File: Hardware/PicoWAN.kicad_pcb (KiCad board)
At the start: 2 copper layers, 50.8 x 22.9 mm, 9 parts, among them J1 Conn_Battery, J3 Conn_left, J4 Conn_right, P1 USB_C_Plug_USB2.0

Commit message: init select footprints
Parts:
- added AE1: Antenna_Shield, Jumper:SolderJumper-2_P1.3mm_Bridged2Bar_Pad1.0x1.5mm, F.Cu at (175.8, 98.0)
- added C1: 22pF, Capacitor_SMD:C_0805_2012Metric, F.Cu at (174.2, 62.7)
- added C10: 0.1uF, Capacitor_SMD:C_0805_2012Metric, F.Cu at (169.7, 61.6)
- added C11: 0.1uF, Capacitor_SMD:C_0805_2012Metric, F.Cu at (172.2, 50.6)
- added C12: 0.1uF, Capacitor_SMD:C_0805_2012Metric, F.Cu at (172.2, 53.6)
- added C13: 0.1uF, Capacitor_SMD:C_0805_2012Metric, F.Cu at (164.9, 58.6)
- added C14: 0.1uF, Capacitor_SMD:C_0805_2012Metric, F.Cu at (159.7, 66.5)
- added C15: 0.1uF, Capacitor_SMD:C_0805_2012Metric, F.Cu at (165.3, 61.6)
- added C16: 10uF, Capacitor_SMD:C_0805_2012Metric, F.Cu at (169.4, 58.6)
- added C17: 10uF, Capacitor_SMD:C_0805_2012Metric, F.Cu at (176.7, 50.6)
- added C18: 0.1uF, Capacitor_SMD:C_0805_2012Metric, F.Cu at (176.7, 53.6)
- added C19: 0.1uF, Capacitor_SMD:C_0805_2012Metric, F.Cu at (165.3, 64.6)
- added C2: 22pF, Capacitor_SMD:C_0805_2012Metric, F.Cu at (178.3, 56.6)
- added C3: 1uF, Capacitor_SMD:C_0805_2012Metric, F.Cu at (174.2, 59.7)
- added C4: 0.1uF, Capacitor_SMD:C_0805_2012Metric, F.Cu at (169.7, 64.6)
- added C5: 4.7uF, Capacitor_SMD:C_0805_2012Metric, F.Cu at (164.2, 67.7)
- added C6: 0.1uF, Capacitor_SMD:C_0805_2012Metric, F.Cu at (173.8, 56.6)
- added C7: 1uF, Capacitor_SMD:C_0805_2012Metric, F.Cu at (159.7, 69.5)
- added C8: 1uF, Capacitor_SMD:C_0805_2012Metric, F.Cu at (178.6, 59.7)
- added C9: 0.1uF, Capacitor_SMD:C_0805_2012Metric, F.Cu at (168.6, 67.7)
- added D1: MBR120, Diode_SMD:D_SOD-123F, F.Cu at (167.3, 50.8)
- added D2: LED, LED_SMD:LED_0805_2012Metric_Pad1.15x1.40mm_HandSolder, F.Cu at (160.7, 63.4)
- added D3: LED, LED_SMD:LED_0805_2012Metric, F.Cu at (181.1, 50.6)
- added R1: 100K, Resistor_SMD:R_0805_2012Metric, F.Cu at (181.1, 53.6)
- added R10: 10K, Resistor_SMD:R_0805_2012Metric, F.Cu at (150.1, 58.4)
- added R11: 5K1, Resistor_SMD:R_0805_2012Metric, F.Cu at (156.6, 52.7)
- added R12: 5K1, Resistor_SMD:R_0805_2012Metric, F.Cu at (154.5, 58.4)
- added R2: 1K, Resistor_SMD:R_0805_2012Metric, F.Cu at (182.7, 56.6)
- added R3: 10K, Resistor_SMD:R_0805_2012Metric, F.Cu at (173.1, 67.6)
- added R4: 27, Resistor_SMD:R_0805_2012Metric, F.Cu at (178.6, 62.6)
- added R5: 27, Resistor_SMD:R_0805_2012Metric, F.Cu at (183.1, 59.5)
- added R6: 2K, Resistor_SMD:R_0805_2012Metric, F.Cu at (177.5, 65.6)
- added R7: 1K, Resistor_SMD:R_0805_2012Metric, F.Cu at (183.0, 62.6)
- added R8: 10K, Resistor_SMD:R_0805_2012Metric, F.Cu at (177.5, 68.6)
- added R9: 1K, Resistor_SMD:R_0805_2012Metric, F.Cu at (181.9, 65.6)
- added U1: AP2112K-3.3, Package_TO_SOT_SMD:SOT-23-5, F.Cu at (138.4, 92.5)
- added U2: RP2040, Package_DFN_QFN:QFN-56-1EP_7x7mm_P0.4mm_EP5.6x5.6mm_ThermalVias, F.Cu at (148.1, 92.7)
- added U3: MCP73831-2-OT, Package_TO_SOT_SMD:SOT-23-5, F.Cu at (138.4, 98.3)
- added U4: W25Q32JVZP, Package_SON:WSON-8-1EP_6x5mm_P1.27mm_EP3.4x4.3mm, F.Cu at (134.9, 71.4)
- added U5: RFM95W-868S2, RF_Module:HOPERF_RFM9XW_SMD, F.Cu at (163.8, 92.7)
- G***: moved to B.Cu
- moved P1 8.14 mm to (131.8, 93.2)
- moved J1 7.88 mm to (137.4, 84.1)
- turned G*** to 180 degrees
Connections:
- J3 pad 10: /A5 -> /D25
- J3 pad 11: /SCK -> /SCK_0
- J3 pad 12: /MOSI -> /COPI_0
- J3 pad 13: /MISO -> /CIPO_0
- J3 pad 16: GND -> /D4
- J3 pad 3: /AREF -> +3V3
- J3 pad 9: /A4 -> /D24

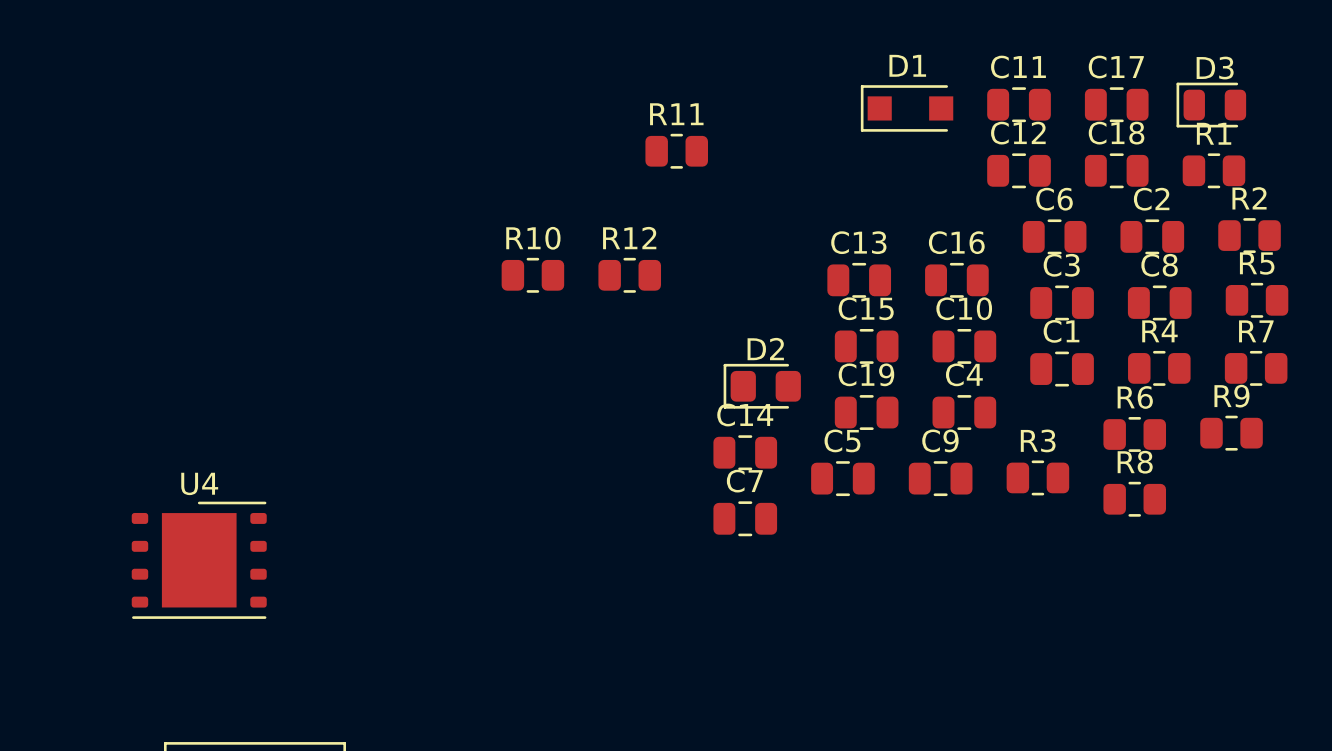
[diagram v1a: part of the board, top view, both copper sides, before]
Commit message: update to 0603
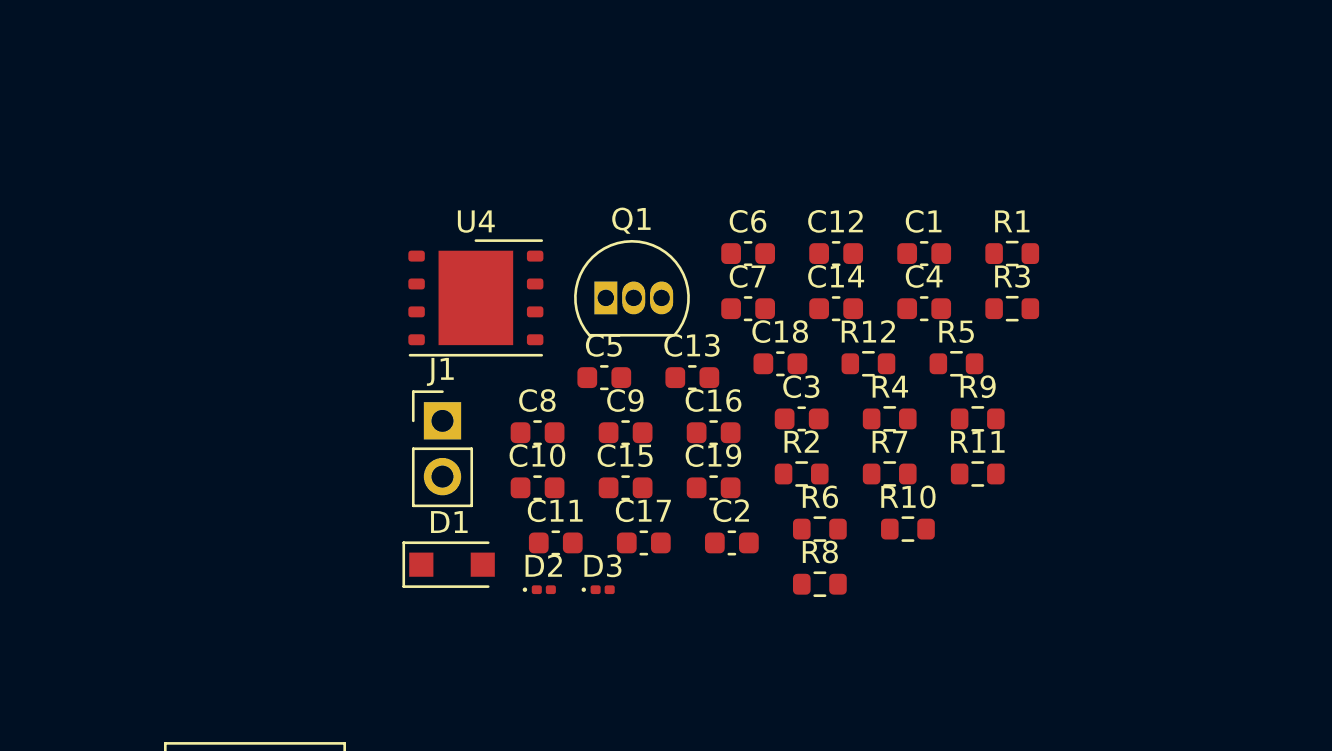
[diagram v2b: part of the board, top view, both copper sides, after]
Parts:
- added J1: Battery, Connector_PinHeader_2.54mm:PinHeader_1x02_P2.54mm_Vertical, F.Cu at (146.0, 65.0)
- added Q1: DMG3415U-7, Package_TO_SOT_THT:TO-92L_Inline, F.Cu at (153.4, 59.4)
- C1, C10, C11, C12, C13, C14, C15, C16, C17, C18, C19, C2, C3, C4, C5, C6, C7, C8, C9: footprint Capacitor_SMD:C_0805_2012Metric -> Capacitor_SMD:C_0603_1608Metric
- D2: footprint LED_SMD:LED_0805_2012Metric_Pad1.15x1.40mm_HandSolder -> LED_SMD:LED_0201_0603Metric
- D3: footprint LED_SMD:LED_0805_2012Metric -> LED_SMD:LED_0201_0603Metric
- R1, R10, R11, R12, R2, R3, R4, R5, R6, R7, R8, R9: footprint Resistor_SMD:R_0805_2012Metric -> Resistor_SMD:R_0603_1608Metric
- moved D3 35.6 mm to (153.2, 72.7)
- moved D1 29.5 mm to (146.4, 71.6)
- moved C17 29.4 mm to (155.1, 70.6)
- moved C11 29.0 mm to (151.1, 70.6)
- moved C8 28.9 mm to (150.3, 65.6)
- moved C2 23.7 mm to (159.1, 70.6)
- moved R2 23.1 mm to (162.3, 67.4)
- moved R10 20.6 mm to (167.2, 70.0)
- moved C10 20.5 mm to (150.3, 68.1)
- moved R11 20.1 mm to (170.3, 67.4)
- moved C18 17.7 mm to (161.3, 62.4)
- moved R7 17.4 mm to (166.3, 67.4)
- moved U4 17.4 mm to (147.5, 59.4)
- moved R6 15.0 mm to (163.1, 70.0)
- moved R8 14.9 mm to (163.1, 72.5)
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
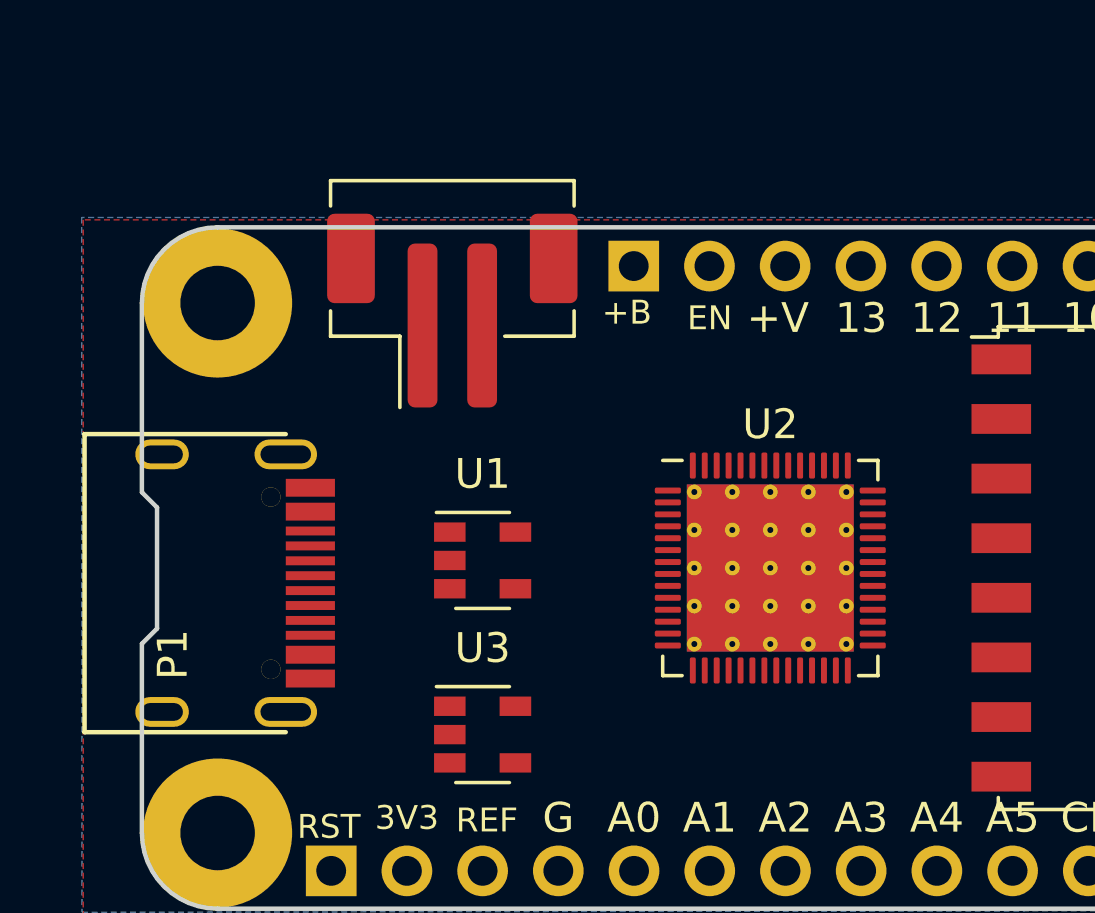
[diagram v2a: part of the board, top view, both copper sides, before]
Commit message: update footprint RP2040
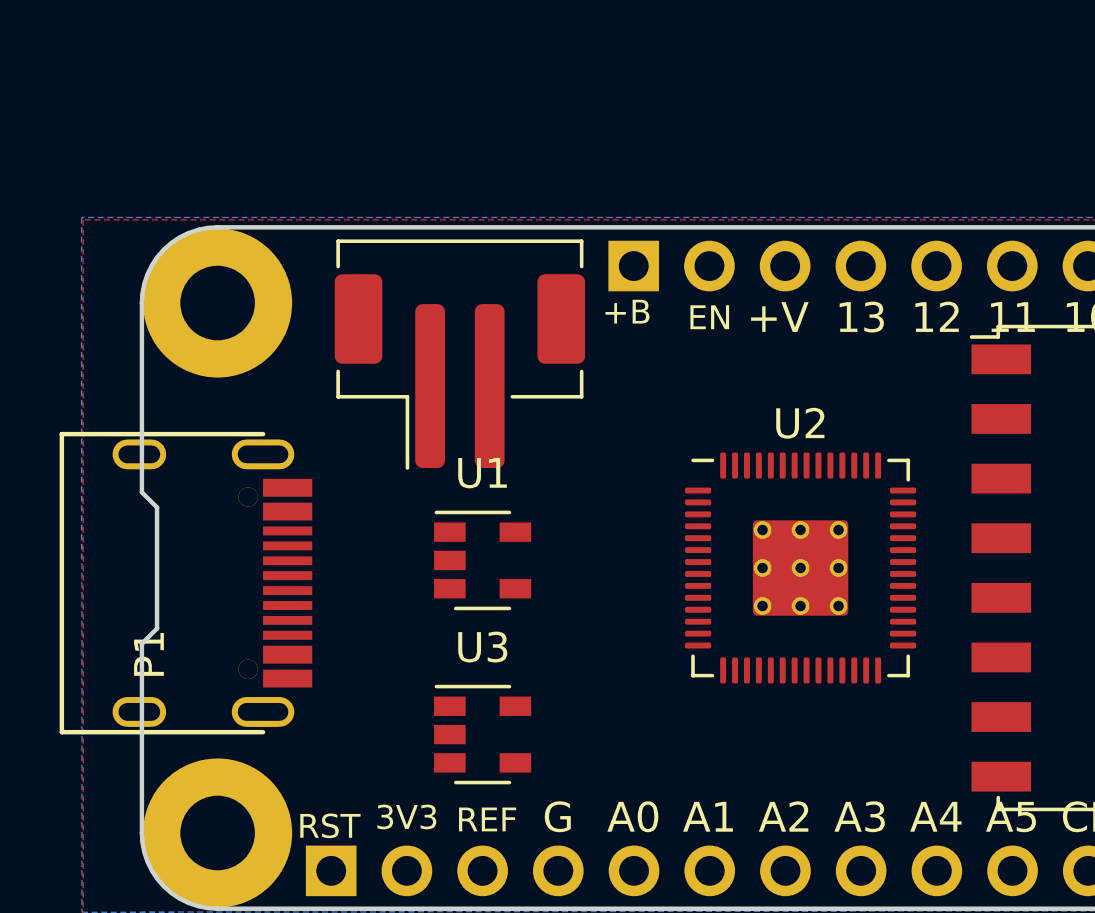
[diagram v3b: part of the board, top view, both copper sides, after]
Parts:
- U2: footprint Package_DFN_QFN:QFN-56-1EP_7x7mm_P0.4mm_EP5.6x5.6mm_ThermalVias -> MCU_RaspberryPi_and_Boards:RP2040-QFN-56
- moved J1 2.05 mm to (137.7, 86.1)
- moved U2 1.02 mm to (149.1, 92.7)
- moved P1 0.76 mm to (131.1, 93.2)

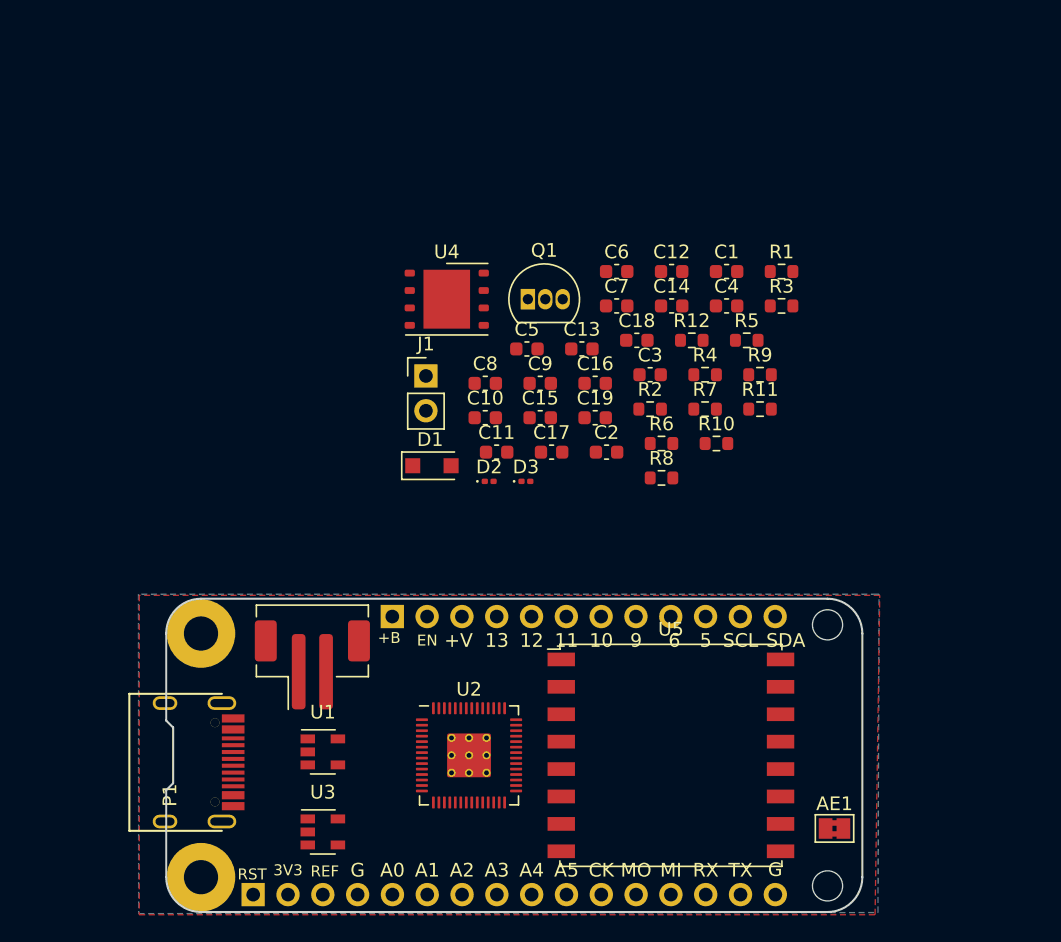
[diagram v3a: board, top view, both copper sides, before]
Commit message: add libraries intialize floor plan
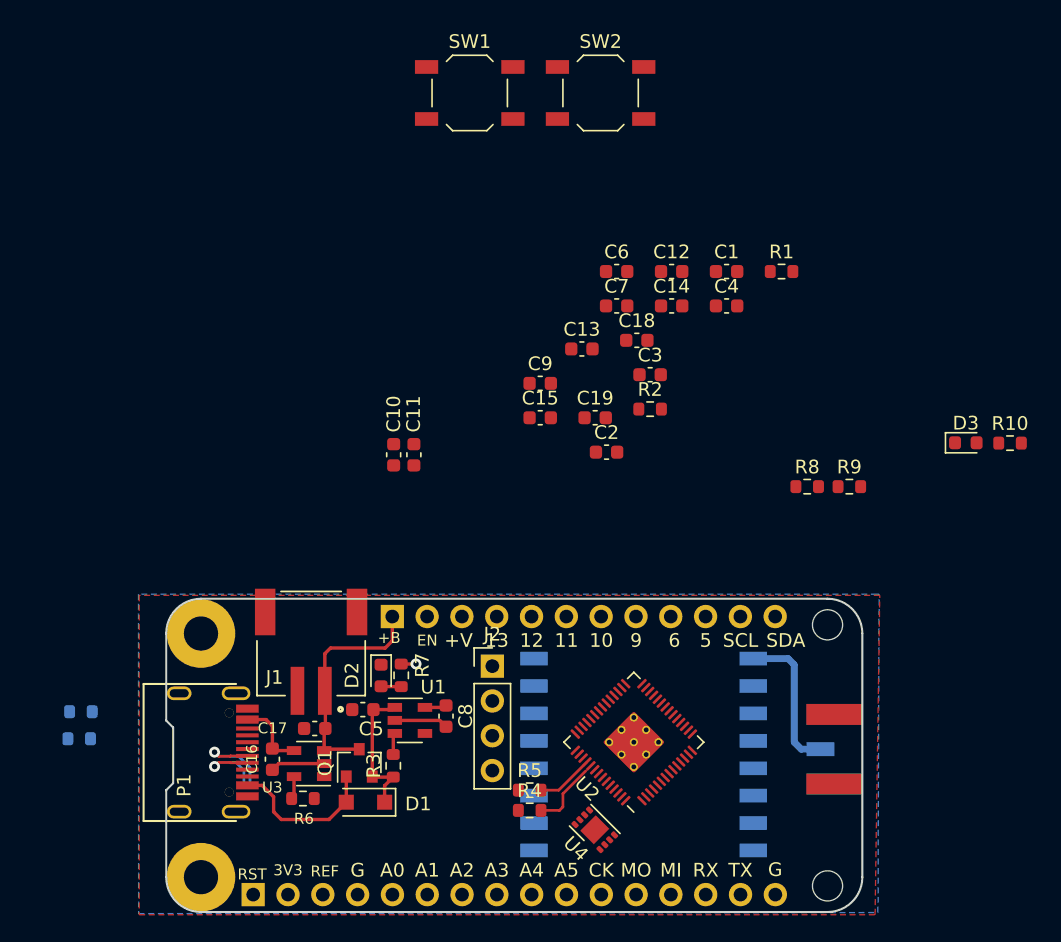
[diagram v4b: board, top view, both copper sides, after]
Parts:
- removed the J1 at (146.0, 65.0)
- removed the J1 at (137.7, 86.1)
- added J1: Battery, pico-wan:JST_S2B-PH-SM4-TB(LF)(SN), F.Cu at (137.6, 88.0)
- added J2: SWD, Connector_PinHeader_2.54mm:PinHeader_1x04_P2.54mm_Vertical, F.Cu at (150.8, 86.2)
- added SW1: BOOT, Button_Switch_SMD:SW_SPST_TL3342, F.Cu at (149.2, 44.4)
- added SW2: RESET, Button_Switch_SMD:SW_SPST_TL3342, F.Cu at (158.7, 44.4)
- AE1: footprint Jumper:SolderJumper-2_P1.3mm_Bridged2Bar_Pad1.0x1.5mm -> pico-wan:SMA_EDGE; moved to B.Cu
- D2, D3: footprint LED_SMD:LED_0201_0603Metric -> LED_SMD:LED_0603_1608Metric
- Q1: footprint Package_TO_SOT_THT:TO-92L_Inline -> Package_TO_SOT_SMD:SOT-23
- R11, R12, U5: moved to B.Cu
- U4: value W25Q32JVZP -> W25Q16JV; footprint Package_SON:WSON-8-1EP_6x5mm_P1.27mm_EP3.4x4.3mm -> Package_SON:SON-8-1EP_3x2mm_P0.5mm_EP1.4x1.6mm
- moved R11 54.3 mm to (120.8, 89.5), turned to 180 degrees
- moved R12 53.3 mm to (120.7, 91.5), turned to 180 degrees
- moved R3 43.9 mm to (143.6, 93.5), turned to 90 degrees
- moved U4 40.2 mm to (158.3, 98.1), turned to 135 degrees
- moved R6 36.8 mm to (137.0, 95.9)
- moved R5 36.4 mm to (153.5, 95.2)
- moved C16 36.2 mm to (134.8, 93.0), turned to 270 degrees
- moved Q1 36.0 mm to (141.1, 93.3), turned to 90 degrees
- moved R4 34.3 mm to (153.5, 96.7)
- moved D3 32.2 mm to (185.3, 69.9)
- moved R7 29.5 mm to (144.2, 86.9), turned to 270 degrees
- moved C5 28.9 mm to (141.3, 89.4), turned to 180 degrees
- moved C17 26.6 mm to (137.8, 90.8), turned to 180 degrees
- moved D1 25.0 mm to (141.5, 96.1), turned to 180 degrees
- moved C8 24.4 mm to (147.4, 89.8), turned to 270 degrees
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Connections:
- Q1 pad 1: Net-(C5-Pad1) -> VBUS
- Q1 pad 2: VBUS -> Net-(C5-Pad1)
- R9 pad 1: /USB_BOOT -> /QSPI_CS
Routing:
- net +BATT: track 0.00 -> 16.8 mm
- net VBUS: track 0.00 -> 16.6 mm
- net Net-(AE1-Pad1): track 0.00 -> 10.9 mm
- net Net-(C5-Pad1): track 0.00 -> 10.2 mm
- net GND: track 0.00 -> 7.90 mm
- net /D-: track 0.00 -> 6.76 mm, vias 0 -> 1
- net /D+: track 0.00 -> 6.20 mm, vias 0 -> 1
- net Net-(R4-Pad2): track 0.00 -> 5.02 mm
- net Net-(R5-Pad2): track 0.00 -> 4.21 mm
- net Net-(R6-Pad1): track 0.00 -> 1.67 mm
- net +3V3: track 0.00 -> 1.60 mm
- net /EN: track 0.00 -> 1.58 mm
- net Net-(D2-Pad2): track 0.00 -> 1.48 mm
- net Net-(R7-Pad1): track 0.00 -> 1.08 mm, vias 0 -> 1

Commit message: Change_footprint
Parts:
- added Y1: 12Mhz, Crystal:Crystal_SMD_2520-4Pin_2.5x2.0mm, F.Cu at (168.1, 88.2)
- C10, C11, C12, C13, C14, C15, C16, C17, C19, C3, C4, C5, C6, C7, C8, C9: footprint Capacitor_SMD:C_0603_1608Metric -> Capacitor_SMD:C_0402_1005Metric
- C18: footprint Capacitor_SMD:C_0603_1608Metric -> Capacitor_SMD:C_0402_1005Metric; moved to B.Cu
- R10, R3, R4, R5, R7, R8, R9: footprint Resistor_SMD:R_0603_1608Metric -> Resistor_SMD:R_0402_1005Metric
- R11, R12: moved to F.Cu
- R2: footprint Resistor_SMD:R_0603_1608Metric -> Resistor_SMD:R_0603_1608Metric_Pad1.05x0.95mm_HandSolder
- moved R1 51.2 mm to (138.9, 96.5)
- moved R10 43.2 mm to (149.4, 88.2), turned to 90 degrees
- moved C12 39.6 mm to (163.3, 97.0), turned to 45 degrees
- moved D3 39.0 mm to (150.6, 87.7), turned to 270 degrees
- moved R9 38.7 mm to (147.9, 98.7), turned to 180 degrees
- moved C6 38.4 mm to (157.2, 95.7), turned to 225 degrees
- moved C7 37.9 mm to (162.0, 97.7), turned to 315 degrees
- moved C4 35.4 mm to (155.1, 92.9), turned to 135 degrees
- moved C14 34.5 mm to (166.0, 94.3), turned to 45 degrees
- moved C13 33.4 mm to (164.7, 95.7), turned to 225 degrees
- moved C19 31.4 mm to (157.0, 99.4), turned to 315 degrees
- moved R8 30.1 mm to (160.4, 100.0), turned to 180 degrees
- moved C1 29.1 mm to (166.3, 86.5), turned to 45 degrees
- moved C18 25.6 mm to (151.8, 86.1), turned to 90 degrees
- moved C11 25.1 mm to (163.7, 87.5), turned to 135 degrees
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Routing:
- net /D+: track 6.20 -> 37.2 mm, vias 1 -> 0
- net /D-: track 6.76 -> 35.5 mm, vias 1 -> 0
- net /QSPI_CS: track 0.00 -> 16.7 mm, vias 0 -> 2
- net +BATT: track 16.8 -> 4.53 mm
- net VBUS: track 16.6 -> 28.4 mm
- net Net-(C1-Pad1): track 0.00 -> 6.27 mm
- net Net-(C2-Pad1): track 0.00 -> 4.93 mm
- net Net-(P1-PadB5): track 0.00 -> 4.38 mm
- net Net-(R4-Pad2): track 5.02 -> 1.66 mm
- net GND: track 7.90 -> 4.73 mm
- net Net-(R5-Pad2): track 4.21 -> 1.88 mm
- net Net-(P1-PadA5): track 0.00 -> 2.27 mm
- net Net-(C5-Pad1): track 10.2 -> 12.2 mm
- net Net-(R2-Pad2): track 0.00 -> 1.97 mm
- net Net-(R6-Pad1): track 1.67 -> 0.00 mm
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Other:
- net class Default: clearance 0.2 -> 0.1; trace_width 0.3 -> 0.25
- net class Source added: clearance 0.1, trace_width 0.3, via_dia 0.8, via_drill 0.4
- rule trace_clearance: 0.2 -> 0.1
